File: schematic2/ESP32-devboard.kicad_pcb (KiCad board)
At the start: 2 copper layers, 100 x 100 mm, 162 parts, among them J1 CON16x1-LEFT, J10 Screw_Terminal_01x12, J11 Screw_Terminal_01x03, J2 CON16x1-RIGHT, J3 GT-USB-7010ASV, J4 Screw_Terminal_01x09, J5 Screw_Terminal_01x03, J6 Screw_Terminal_01x03, J7 Screw_Terminal_01x08, J8 Screw_Terminal_01x03, J9 Screw_Terminal_01x04, Q1 SS8050 200-350, Q10 MMBT3904 100-300, Q11 MMBT3904 100-300, Q12 AO3401A, Q13 MMBT3904 100-300, Q14 AO3401A, Q16 HL3400, Q2 HL3400, Q3 SS8050 200-350, Q4 HL3400, Q5 HL3400, Q7 MMBT3904 100-300, Q8 AO3401A, Q9 AO3401A, U1 ESP32-WROOM-E, U13 LTV-217-B-G, U14 LTV-217-B-G, U15 LTV-217-B-G, U16 LTV-217-B-G, U17 LTV-217-B-G, U18 LTV-217-B-G, U19 LTV-217-B-G, U2 CP2102N-Axx-xQFN28, U20 LTV-217-B-G, U21 LTV-217-B-G, U22 LTV-217-B-G, U23 LTV-217-B-G, U24 LTV-217-B-G, U25 LTV-217-B-G, U26 LTV-217-B-G, U27 LTV-217-B-G, U28 LTV-217-B-G, U29 CD4051BM96, U3 AMS1117-3.3, U4 XL1509, U5 CD4051BM96

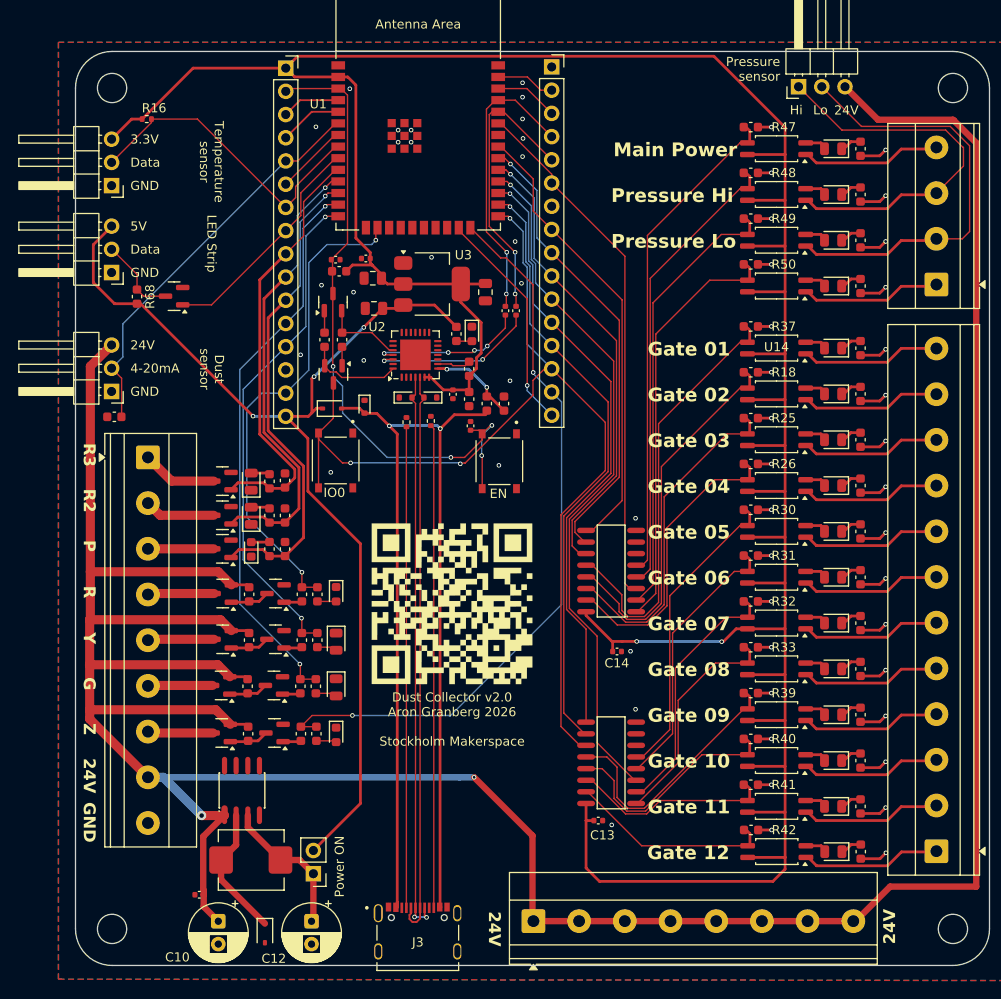
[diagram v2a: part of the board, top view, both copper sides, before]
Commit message: Add ESD protection and other safety improvements
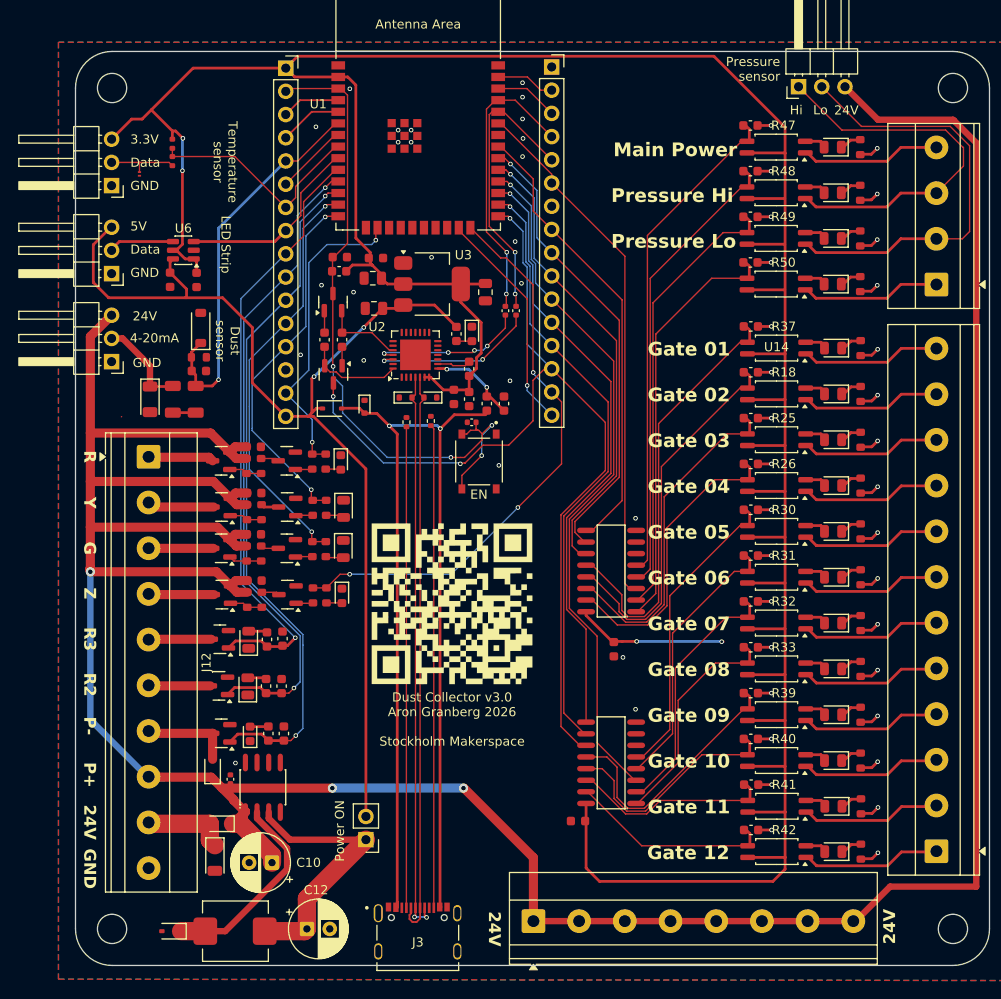
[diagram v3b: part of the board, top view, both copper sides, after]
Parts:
- removed J4: Screw_Terminal_01x09, TerminalBlock_Phoenix:TerminalBlock_Phoenix_MKDS-1,5-9_1x09_P5.00mm_Horizontal
- removed Q11, Q13, Q7: MMBT3904 100-300, PCM_JLCPCB:Q_SOT-23
- removed Q12, Q14, Q8: AO3401A, PCM_JLCPCB:Q_SOT-23
- removed Q16: HL3400, PCM_JLCPCB:Q_SOT-23
- removed R19, R57, R60: 2K2(5%), Capacitor_SMD:C_0603_1608Metric
- removed R38, R56, R58, R59, R61, R62, R68: 10K(1%), Capacitor_SMD:C_0603_1608Metric
- removed S1: TS-1187A-B-A-B, Switch_Custom:SW_TS-1187A-B-A-B
- added C15: 100nF, PCM_JLCPCB:C_0603, F.Cu at (128.5, 100.0)
- added C16: 100nF, PCM_JLCPCB:C_0603, F.Cu at (125.3, 90.0)
- added C17: 100nF, PCM_JLCPCB:C_0603, F.Cu at (128.2, 90.0)
- added C18: 1uF, PCM_JLCPCB:C_0603, F.Cu at (134.6, 113.3)
- added C19: 1uF, PCM_JLCPCB:C_0603, F.Cu at (134.5, 117.8)
- added C20: 1uF, PCM_JLCPCB:C_0603, F.Cu at (134.6, 122.9)
- added C22: 1uF, PCM_JLCPCB:C_0603, F.Cu at (134.5, 108.3)
- added D31: 1N5819WS, PCM_JLCPCB:D_SOD-323, F.Cu at (130.8, 149.5)
- added D34: SMF26A, PCM_JLCPCB:D_SOD-123FL, F.Cu at (130.2, 153.2)
- added D35: SMF26A, PCM_JLCPCB:D_SOD-123FL, F.Cu at (123.2, 103.1)
- added D36: 1N5819WS, PCM_JLCPCB:D_SOD-323, F.Cu at (130.0, 143.5)
- added D38: TT0421SAX, PCM_JLCPCB:D_DFN0603-2L, F.Cu at (122.0, 78.4)
- added D39: BZT52B3V3, PCM_JLCPCB:D_SOD-123, F.Cu at (128.7, 95.2)
- added J12: Screw_Terminal_01x10, TerminalBlock_Phoenix:TerminalBlock_Phoenix_MKDS-1,5-10_1x10_P5.00mm_Horizontal, F.Cu at (123.0, 109.3)
- added Q15: AO3401A, PCM_JLCPCB:Q_SOT-23, F.Cu at (131.0, 114.8)
- added Q17: MMBT3904 100-300, PCM_JLCPCB:Q_SOT-23, F.Cu at (138.1, 119.4)
- added Q18: AO3401A, PCM_JLCPCB:Q_SOT-23, F.Cu at (131.0, 119.4)
- added Q19: MMBT3904 100-300, PCM_JLCPCB:Q_SOT-23, F.Cu at (138.2, 124.4)
- added Q20: AO3401A, PCM_JLCPCB:Q_SOT-23, F.Cu at (131.0, 124.4)
- added Q6: MMBT3904 100-300, PCM_JLCPCB:Q_SOT-23, F.Cu at (138.2, 114.8)
- added R23: 300Ω, PCM_JLCPCB:R_1206, F.Cu at (125.7, 103.1)
- added R66: 120Ω, PCM_JLCPCB:R_0603, F.Cu at (128.5, 98.5)
- added R67: 3.3kΩ, PCM_JLCPCB:R_0402, F.Cu at (125.6, 75.1)
- added R69: 300Ω, PCM_JLCPCB:R_1206, F.Cu at (128.2, 103.1)
- added R70: 2.2kΩ, PCM_JLCPCB:R_0603, F.Cu at (142.4, 114.9)
- added R71: 10kΩ, PCM_JLCPCB:R_0603, F.Cu at (140.9, 114.9)
- added R72: 15kΩ, PCM_JLCPCB:R_0603, F.Cu at (135.4, 115.4)
- added R73: 10kΩ, PCM_JLCPCB:R_0603, F.Cu at (133.8, 115.4)
- added R74: 2.2kΩ, PCM_JLCPCB:R_0603, F.Cu at (142.4, 119.5)
- added R75: 10kΩ, PCM_JLCPCB:R_0603, F.Cu at (140.9, 119.5)
- added R76: 15kΩ, PCM_JLCPCB:R_0603, F.Cu at (135.3, 119.9)
- added R77: 10kΩ, PCM_JLCPCB:R_0603, F.Cu at (133.7, 119.9)
- added R78: 2.2kΩ, PCM_JLCPCB:R_0603, F.Cu at (142.5, 124.5)
- added R79: 10kΩ, PCM_JLCPCB:R_0603, F.Cu at (141.0, 124.5)
- added R80: 15kΩ, PCM_JLCPCB:R_0603, F.Cu at (135.4, 125.0)
- added R81: 10kΩ, PCM_JLCPCB:R_0603, F.Cu at (133.8, 125.0)
- added U6: SN74LVC1T45DBVR, Package_TO_SOT_SMD:SOT-23-6, F.Cu at (126.8, 86.8)
- C13, C14, C2, C4, C5: value 0.1uF/50V(10%) -> 100nF; footprint Capacitor_SMD:C_0402_1005Metric -> PCM_JLCPCB:C_0603
- R16: value 5K1(1%) -> 100Ω; footprint Resistor_SMD:R_0402_1005Metric -> PCM_JLCPCB:R_0402
- R17: value 120R(1%) -> 10kΩ; footprint Capacitor_SMD:C_0603_1608Metric -> PCM_JLCPCB:R_0603
- R20: value 10K(1%) -> 10kΩ; footprint Capacitor_SMD:C_0603_1608Metric -> PCM_JLCPCB:R_0603
- R21: value 2K2(5%) -> 15kΩ; footprint Capacitor_SMD:C_0603_1608Metric -> PCM_JLCPCB:R_0603
- R22: value 10K(1%) -> 2.2kΩ; footprint Capacitor_SMD:C_0603_1608Metric -> PCM_JLCPCB:R_0603
- R24, R27, R28, R29, R34, R35, R36, R43, R44, R45, R46, R51, R52, R53, R54, R55: value 2K2(5%) -> 4.7kΩ; footprint Capacitor_SMD:C_0603_1608Metric -> PCM_JLCPCB:R_0603
- moved D1 20.2 mm to (134.1, 139.7)
- moved R12 20.2 mm to (136.1, 139.6)
- moved R63 20.2 mm to (137.8, 139.6)
- moved Q2 20.2 mm to (130.9, 139.6)
- moved C14 19.0 mm to (170.0, 149.2), turned to 180 degrees
- moved C13 18.8 mm to (173.9, 130.4), turned to -90 degrees
- moved R13 18.7 mm to (135.8, 134.4)
- moved R64 18.7 mm to (137.5, 134.4)
- moved D5 18.7 mm to (133.8, 134.5)
- moved Q4 18.7 mm to (130.7, 134.4)
- moved D13 17.3 mm to (133.9, 129.4)
- moved Q5 17.3 mm to (130.8, 129.3)
- moved R15 17.3 mm to (135.9, 129.3)
- moved R65 17.3 mm to (137.6, 129.2)
- moved R20 16.1 mm to (140.9, 109.9)
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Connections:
- J1 pad 5: /Dust sensor loop -> /IO34
- J6 pad 2: /IO32 -> /Onewire bus
- Q9 pad 1: Net-(Q10-C) -> Net-(Q9-G)
- R16 pad 1: /IO32 -> /Onewire bus
- R16 pad 2: /3.3V -> /IO32
- R17 pad 1: GND -> /24V
- R17 pad 2: /Dust sensor loop -> Net-(Q9-G)
- R20 pad 1: Net-(Q10-C) -> Net-(Q10-B)
- R20 pad 2: /24V -> /IO13
- R21 pad 1: Net-(D7-Pad2) -> Net-(Q10-C)
- R21 pad 2: /IO13 -> Net-(Q9-G)
- R22 pad 1: /IO13 -> Net-(D7-Pad2)
- R22 pad 2: Net-(Q10-B) -> /IO13
- U1 pad 6: /Dust sensor loop -> /IO34
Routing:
- net /IO34: track 0.00 -> 42.5 mm, vias 0 -> 1
- net /Dust sensor loop: track 43.8 -> 10.5 mm
- net /IO27: track 52.5 -> 75.1 mm, vias 1 -> 2
- net /IO26: track 49.8 -> 71.0 mm, vias 1 -> 2
- net /IO25: track 46.7 -> 66.2 mm, vias 0 -> 1
- net /IO13: track 53.6 -> 34.2 mm
- net /IO2: track 81.5 -> 63.1 mm, vias 2 -> 3
- net /3.3V: track 339.7 -> 357.1 mm, vias 2 -> 4
- net /IO14: track 61.5 -> 46.0 mm
- net /IO12: track 55.0 -> 39.9 mm
- net GND: track 63.9 -> 49.9 mm, vias 57 -> 56
- net Net-(JP2-A): track 15.9 -> 29.4 mm
- net /IO32: track 34.4 -> 24.8 mm
- net /24V_RAW: track 0.00 -> 9.32 mm
- net /Onewire bus: track 0.00 -> 7.86 mm
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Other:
- board text added: "Dust Collector v3.0 Aron Granberg 2026 Stockholm Makerspace"
- board text added: "P+"
- board text added: "P-"
- board text removed: "Dust Collector v2.0 Aron Granberg 2026 Stockholm Makerspace"
- board text removed: "IO0"
- board text removed: "P"

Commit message: Final tweaks. Ordered from JLCPCB
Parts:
- C10, C12: footprint Capacitor_THT:CP_Radial_D6.3mm_P2.50mm -> Capacitor_THT:CP_Radial_D10.0mm_P5.00mm
- C11: value 0.1uF/50V(10%) -> 100nF; footprint Capacitor_SMD:C_0402_1005Metric -> PCM_JLCPCB:C_0603
- R1, R2, R63, R64, R65, R9: value 10K(1%) -> 10kΩ; footprint Capacitor_SMD:C_0603_1608Metric -> PCM_JLCPCB:R_0603
- R10, R12, R13, R15, R5: value 2K2(5%) -> 2.2kΩ; footprint Capacitor_SMD:C_0603_1608Metric -> PCM_JLCPCB:R_0603
- R18, R25, R26, R3, R30, R31, R32, R33, R37, R39, R4, R40, R41, R42, R47, R48, R49, R50: footprint Capacitor_SMD:C_0603_1608Metric -> PCM_JLCPCB:R_0603
- moved C12 23.0 mm to (147.0, 139.0), turned to 180 degrees
- moved JP2 20.1 mm to (146.8, 131.1)
- moved G*** 3.49 mm to (159.0, 123.3)
- moved L1 2.01 mm to (130.5, 161.4)
- moved D8 1.31 mm to (124.2, 161.4), turned to 90 degrees
- moved C10 1.05 mm to (136.6, 154.8), turned to 0 degrees
- moved C11 0.18 mm to (132.0, 144.8), turned to -90 degrees
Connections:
- net Net-(U4-OUTPUT) renamed /Switch24V
- C11 pad 1: /24V -> GND
- C11 pad 2: GND -> /24V
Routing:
- net Net-(JP2-A): track 29.4 -> 49.9 mm
- net /5V: track 117.9 -> 97.8 mm
- net /Switch24V: track 22.0 -> 26.8 mm
- net /3.3V: track 357.1 -> 360.5 mm
- net /24V: track 350.5 -> 352.0 mm
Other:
- board text added: "Power"
- board text removed: "Power ON"
